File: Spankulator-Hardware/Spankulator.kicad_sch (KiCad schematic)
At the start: 99 parts, among them J1 3.5mm Jack, J12 Arduino Socket, J13 Arduino Socket, J2 2x5 Header, J3 3.5mm Jack, J4 3.5mm Jack, J5 3.5mm Jack, J6 3.5mm Jack, J7 2x5 Header, J9 Display Header, Q1 2N3904, SW1 Adj, SW2 Push Button, SW3 Push Button, SW4 Push Button, SW5 Push Button, SW6 Push Button, SW7 Push Button, SW8 Push Button, U1 TL072CP, U2 CD4013BE, U3 TL072CP, U4 MC78L05_TO92, U5 LP2950-3.3_TO92, U6 MAX7480, U7 MB85RC256, U8 MCP6002-E/P

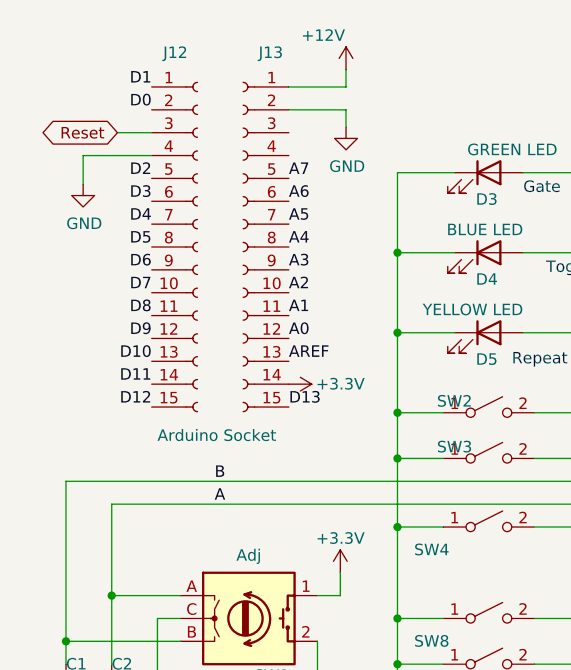
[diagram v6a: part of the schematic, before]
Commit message: Adds pullup resistors to rotary encoder.
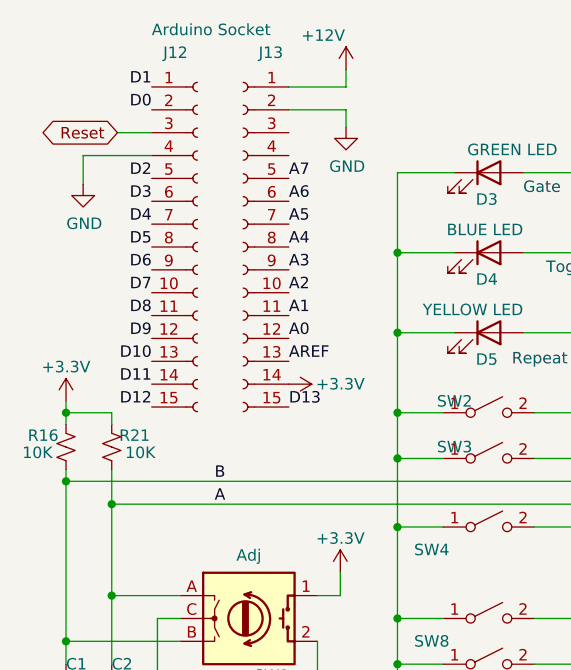
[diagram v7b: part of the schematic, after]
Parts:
- added R16, R21: 10K, Resistor_THT:R_Axial_DIN0207_L6.3mm_D2.5mm_P10.16mm_Horizontal, symbol Device:R_Small_US
- Q1, U5: footprint Package_TO_SOT_THT:TO-92-3_Formed_Leads -> digikey-footprints:TO-92-3_Formed_Leads
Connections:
- net +3V3: now also R16.1, R21.1
- net A: now also R21.2
- net B: now also R16.2
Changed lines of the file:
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@@
   (title_block
     (title "Spankulator")
-    (rev "5.3")
+    (rev "5.4")
     (company "Greenface Labs")
   )
@@
   (junction (at 54.61 60.96) (diameter 0) (color 0 0 0 0)
   )
+  (junction (at 17.78 63.5) (diameter 0) (color 0 0 0 0)
+  )
   (junction (at 96.52 183.515) (diameter 0) (color 0 0 0 0)
   )
@@
   (junction (at 187.96 156.21) (diameter 0) (color 0 0 0 0)
   )
+  (junction (at 17.78 55.88) (diameter 0) (color 0 0 0 0)
+  )
+  (junction (at 22.86 66.04) (diameter 0) (color 0 0 0 0)
+  )
   (junction (at 139.7 55.88) (diameter 0) (color 0 0 0 0)
   )
@@
     (stroke (width 0) (type default) (color 0 0 0 0))
   )
+  (wire (pts (xy 17.78 55.88) (xy 17.78 57.15))
+    (stroke (width 0) (type default) (color 0 0 0 0))
+  )
   (wire (pts (xy 116.84 44.45) (xy 116.84 48.26))
     (stroke (width 0) (type default) (color 0 0 0 0))
@@
     (stroke (width 0) (type default) (color 0 0 0 0))
   )
+  (wire (pts (xy 17.78 55.88) (xy 22.86 55.88))
+    (stroke (width 0) (type default) (color 0 0 0 0))
+  )
   (wire (pts (xy 198.12 63.5) (xy 199.39 63.5))
     (stroke (width 0) (type default) (color 0 0 0 0))
@@
     (stroke (width 0) (type default) (color 0 0 0 0))
   )
+  (wire (pts (xy 17.78 62.23) (xy 17.78 63.5))
+    (stroke (width 0) (type default) (color 0 0 0 0))
+  )
   (wire (pts (xy 123.19 171.45) (xy 123.19 173.99))
     (stroke (width 0) (type default) (color 0 0 0 0))
@@
     (stroke (width 0) (type default) (color 0 0 0 0))
   )
+  (wire (pts (xy 17.78 54.61) (xy 17.78 55.88))
+    (stroke (width 0) (type default) (color 0 0 0 0))
+  )
   (wire (pts (xy 193.04 91.44) (xy 195.58 91.44))
     (stroke (width 0) (type default) (color 0 0 0 0))
@@
     (stroke (width 0) (type default) (color 0 0 0 0))
   )
+  (wire (pts (xy 22.86 62.23) (xy 22.86 66.04))
+    (stroke (width 0) (type default) (color 0 0 0 0))
+  )
   (wire (pts (xy 250.19 24.13) (xy 247.65 24.13))
     (stroke (width 0) (type default) (color 0 0 0 0))
@@
     (stroke (width 0) (type default) (color 0 0 0 0))
   )
+  (wire (pts (xy 22.86 57.15) (xy 22.86 55.88))
+    (stroke (width 0) (type default) (color 0 0 0 0))
+  )
   (wire (pts (xy 138.43 189.23) (xy 142.875 189.23))
     (stroke (width 0) (type default) (color 0 0 0 0))
@@
     (property "Reference" "U5" (id 0) (at 173.99 133.5532 0))
     (property "Value" "LP2950-3.3_TO92" (id 1) (at 173.99 135.8646 0))
-    (property "Footprint" "Package_TO_SOT_THT:TO-92-3_Formed_Leads" (id 2) (at 173.99 133.985 0)
+    (property "Footprint" "digikey-footprints:TO-92-3_Formed_Leads" (id 2) (at 173.99 133.985 0)
       (effects (font (size 1.27 1.27) italic) hide)
     )
@@
     (pin "2")
   )
+  (symbol (lib_id "Device:R_Small_US") (at 17.78 59.69 0) (unit 1)
+    (in_bom yes) (on_board yes)
+    (property "Reference" "R16" (id 0) (at 15.24 58.42 0))
+    (property "Value" "10K" (id 1) (at 14.605 60.325 0))
+    (property "Footprint" "Resistor_THT:R_Axial_DIN0207_L6.3mm_D2.5mm_P10.16mm_Horizontal" (id 2) (at 17.78 59.69 0)
+      (effects (font (size 1.27 1.27)) hide)
+    )
+    (property "Datasheet" "~" (id 3) (at 17.78 59.69 0)
+      (effects (font (size 1.27 1.27)) hide)
+    )
+    (property "Digi-Key Part" "CF14JT10K0CT-ND" (id 4) (at 17.78 59.69 90)
+      (effects (font (size 1.27 1.27)) hide)
+    )
+    (property "LCSC Part #" "C433778" (id 5) (at 17.78 59.69 0)
+      (effects (font (size 1.27 1.27)) hide)
+    )
+    (pin "1")
+    (pin "2")
+  )
   (symbol (lib_id "power:+3.3V") (at 145.415 100.33 0) (unit 1)
     (in_bom yes) (on_board yes)
@@
       (effects (font (size 1.27 1.27)) (justify left))
     )
-    (property "Value" "Arduino Socket" (id 1) (at 27.94 58.42 0)
+    (property "Value" "Arduino Socket" (id 1) (at 27.305 13.335 0)
       (effects (font (size 1.27 1.27)) (justify left))
     )
@@
     (property "Reference" "Q1" (id 0) (at 124.46 134.1841 90))
     (property "Value" "2N3904" (id 1) (at 124.46 136.9592 90))
-    (property "Footprint" "Package_TO_SOT_THT:TO-92-3_Formed_Leads" (id 2) (at 126.365 137.16 0)
+    (property "Footprint" "digikey-footprints:TO-92-3_Formed_Leads" (id 2) (at 126.365 137.16 0)
       (effects (font (size 1.27 1.27) italic) (justify left) hide)
     )
@@
     (pin "7")
   )
+  (symbol (lib_id "power:+3.3V") (at 17.78 54.61 0) (unit 1)
+    (in_bom yes) (on_board yes)
+    (property "Reference" "#PWR019" (id 0) (at 17.78 58.42 0)
+      (effects (font (size 1.27 1.27)) hide)
+    )
+    (property "Value" "+3.3V" (id 1) (at 17.78 50.8 0))
+    (property "Footprint" "" (id 2) (at 17.78 54.61 0)
+      (effects (font (size 1.27 1.27)) hide)
+    )
+    (property "Datasheet" "" (id 3) (at 17.78 54.61 0)
+      (effects (font (size 1.27 1.27)) hide)
+    )
+    (pin "1")
+  )
   (symbol (lib_id "Connector:Conn_01x15_Female") (at 37.465 37.465 0) (mirror y) (unit 1)
     (in_bom yes) (on_board yes)
@@
     (pin "1")
   )
+  (symbol (lib_id "Device:R_Small_US") (at 22.86 59.69 0) (unit 1)
+    (in_bom yes) (on_board yes)
+    (property "Reference" "R21" (id 0) (at 25.4 58.42 0))
+    (property "Value" "10K" (id 1) (at 26.035 60.325 0))
+    (property "Footprint" "Resistor_THT:R_Axial_DIN0207_L6.3mm_D2.5mm_P10.16mm_Horizontal" (id 2) (at 22.86 59.69 0)
+      (effects (font (size 1.27 1.27)) hide)
+    )
+    (property "Datasheet" "~" (id 3) (at 22.86 59.69 0)
+      (effects (font (size 1.27 1.27)) hide)
+    )
+    (property "Digi-Key Part" "CF14JT10K0CT-ND" (id 4) (at 22.86 59.69 90)
+      (effects (font (size 1.27 1.27)) hide)
+    )
+    (property "LCSC Part #" "C433778" (id 5) (at 22.86 59.69 0)
+      (effects (font (size 1.27 1.27)) hide)
+    )
+    (pin "1")
+    (pin "2")
+  )
   (symbol (lib_id "power:GND") (at 48.895 24.13 0) (unit 1)
     (in_bom yes) (on_board yes)
@@
       (reference "#PWR018") (unit 1) (value "GND") (footprint "")
     )
+    (path "/bb74453b-793d-42ed-aa5f-ef411d7ca60f"
+      (reference "#PWR019") (unit 1) (value "+3.3V") (footprint "")
+    )
     (path "/00000000-0000-0000-0000-00005f38ace8"
       (reference "#PWR021") (unit 1) (value "+12V") (footprint "")
@@
     )
     (path "/82f88b33-a287-4e4b-8286-fcbdf9dee6f1"
-      (reference "Q1") (unit 1) (value "2N3904") (footprint "Package_TO_SOT_THT:TO-92-3_Formed_Leads")
+      (reference "Q1") (unit 1) (value "2N3904") (footprint "digikey-footprints:TO-92-3_Formed_Leads")
     )
     (path "/00000000-0000-0000-0000-00005ce0a0b6"
@@
       (reference "R15") (unit 1) (value "10K") (footprint "Resistor_THT:R_Axial_DIN0207_L6.3mm_D2.5mm_P10.16mm_Horizontal")
     )
+    (path "/0a3a5220-544c-4d88-b0d5-a729ed0c0dca"
+      (reference "R16") (unit 1) (value "10K") (footprint "Resistor_THT:R_Axial_DIN0207_L6.3mm_D2.5mm_P10.16mm_Horizontal")
+    )
     (path "/00000000-0000-0000-0000-00005f427c66"
       (reference "R17") (unit 1) (value "324K 1%") (footprint "Resistor_THT:R_Axial_DIN0207_L6.3mm_D2.5mm_P10.16mm_Horizontal")
@@
       (reference "R20") (unit 1) (value "470") (footprint "Resistor_THT:R_Axial_DIN0207_L6.3mm_D2.5mm_P10.16mm_Horizontal")
     )
+    (path "/f3279773-db43-480e-8a82-3aa1f4ab405e"
+      (reference "R21") (unit 1) (value "10K") (footprint "Resistor_THT:R_Axial_DIN0207_L6.3mm_D2.5mm_P10.16mm_Horizontal")
+    )
     (path "/cbb1bb1c-2683-4a4d-a54f-78de9cd60431"
       (reference "R22") (unit 1) (value "10K") (footprint "Resistor_THT:R_Axial_DIN0207_L6.3mm_D2.5mm_P10.16mm_Horizontal")
@@
     )
     (path "/00000000-0000-0000-0000-00006038f82e"
-      (reference "U5") (unit 1) (value "LP2950-3.3_TO92") (footprint "Package_TO_SOT_THT:TO-92-3_Formed_Leads")
+      (reference "U5") (unit 1) (value "LP2950-3.3_TO92") (footprint "digikey-footprints:TO-92-3_Formed_Leads")
     )
     (path "/00000000-0000-0000-0000-00006045cf3c"
